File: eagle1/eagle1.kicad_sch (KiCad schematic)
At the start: 2 parts

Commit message: Select USB-C plug
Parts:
- J1, J2: Manufacturer (none) -> GlobTek, Inc.; Part Number (none) -> PLUG-USBC-121SMT-4BS2S
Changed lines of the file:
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@@
       (effects (font (size 1.27 1.27)) hide)
     )
-    (property "Datasheet" "" (at 104.775 94.615 0)
+    (property "Datasheet" "https://globtek.my.salesforce-sites.com/spec/pdf/2342616/d2760419" (at 104.775 94.615 0)
       (effects (font (size 1.27 1.27)) hide)
     )
-    (property "Manufacturer" "" (at 104.775 94.615 0)
-      (effects (font (size 1.27 1.27)))
+    (property "Manufacturer" "GlobTek, Inc." (at 104.775 94.615 0)
+      (effects (font (size 1.27 1.27)) hide)
     )
-    (property "Part Number" "" (at 104.775 94.615 0)
-      (effects (font (size 1.27 1.27)))
+    (property "Part Number" "PLUG-USBC-121SMT-4BS2S" (at 104.775 94.615 0)
+      (effects (font (size 1.27 1.27)) hide)
     )
-    (property "Description" "" (at 104.775 94.615 0)
-      (effects (font (size 1.27 1.27)))
+    (property "Description" "USB-C (USB TYPE-C) USB 2.0 Plug Connector 24 (12+12 Dummy) Position Surface Mount, Right Angle" (at 104.775 94.615 0)
+      (effects (font (size 1.27 1.27)) hide)
     )
     (pin "A1")
@@
       (effects (font (size 1.27 1.27)) hide)
     )
-    (property "Datasheet" "" (at 204.47 94.615 0)
+    (property "Datasheet" "https://globtek.my.salesforce-sites.com/spec/pdf/2342616/d2760419" (at 204.47 94.615 0)
       (effects (font (size 1.27 1.27)) hide)
     )
+    (property "Manufacturer" "GlobTek, Inc." (at 204.47 94.615 0)
+      (effects (font (size 1.27 1.27)) hide)
+    )
+    (property "Part Number" "PLUG-USBC-121SMT-4BS2S" (at 204.47 94.615 0)
+      (effects (font (size 1.27 1.27)) hide)
+    )
+    (property "Description" "USB-C (USB TYPE-C) USB 2.0 Plug Connector 24 (12+12 Dummy) Position Surface Mount, Right Angle" (at 204.47 94.615 0)
+      (effects (font (size 1.27 1.27)) hide)
+    )

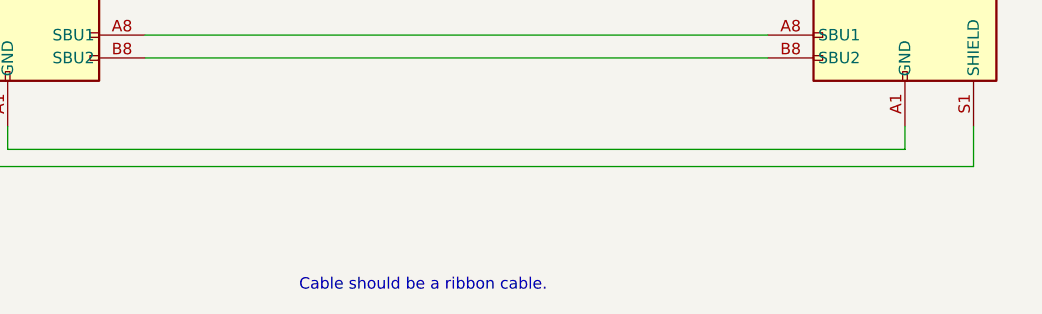
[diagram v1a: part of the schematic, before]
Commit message: Add footprint for Eagle1 USB-C plug
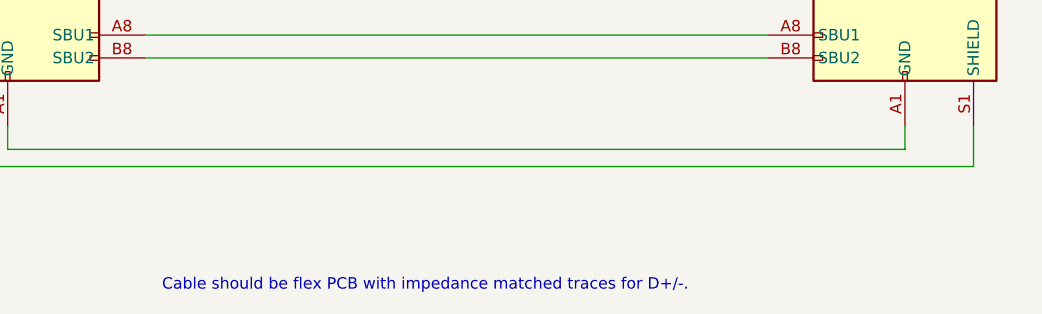
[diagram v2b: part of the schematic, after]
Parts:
- J1, J2: value ~ -> USB-C Plug; footprint (none) -> tycho:PLUG-USBC-121SMT
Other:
- note added: "Cable should be flex PCB with impedance matched traces for D+/-."
- note removed: "Cable should be a ribbon cable."
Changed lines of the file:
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@@
     (effects (font (size 1.27 1.27)) (justify left bottom))
   )
-  (text "Cable should be a ribbon cable." (at 137.16 146.05 0)
+  (text "Cable should be flex PCB with impedance matched traces for D+/-."
+    (at 121.92 146.05 0)
     (effects (font (size 1.27 1.27)) (justify left bottom))
   )
@@
       (effects (font (size 1.27 1.27)))
     )
-    (property "Value" "~" (at 104.775 94.615 0)
-      (effects (font (size 1.27 1.27)))
+    (property "Value" "USB-C Plug" (at 104.775 94.615 0)
+      (effects (font (size 1.27 1.27)) hide)
     )
-    (property "Footprint" "" (at 104.775 94.615 0)
+    (property "Footprint" "tycho:PLUG-USBC-121SMT" (at 104.775 94.615 0)
       (effects (font (size 1.27 1.27)) hide)
     )
@@
       (effects (font (size 1.27 1.27)) (justify right))
     )
-    (property "Value" "~" (at 204.47 94.615 0)
-      (effects (font (size 1.27 1.27)))
-    )
-    (property "Footprint" "" (at 204.47 94.615 0)
+    (property "Value" "USB-C Plug" (at 204.47 94.615 0)
       (effects (font (size 1.27 1.27)) hide)
     )
+    (property "Footprint" "tycho:PLUG-USBC-121SMT" (at 204.47 94.615 0)
+      (effects (font (size 1.27 1.27)) hide)
+    )

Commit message: Add footprint for U261-241N-4BC2LS USB-C plug
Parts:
- J1, J2: Manufacturer GlobTek, Inc. -> XKB Connectivity; Part Number PLUG-USBC-121SMT-4BS2S -> U261-241N-4BC2SS
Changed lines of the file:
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@@
       (effects (font (size 1.27 1.27)) hide)
     )
-    (property "Datasheet" "https://globtek.my.salesforce-sites.com/spec/pdf/2342616/d2760419" (at 104.775 94.615 0)
+    (property "Datasheet" "https://datasheet.lcsc.com/lcsc/2201121830_XKB-Connectivity-U261-241N-4BC2SS_C2938597.pdf" (at 104.775 94.615 0)
       (effects (font (size 1.27 1.27)) hide)
     )
-    (property "Manufacturer" "GlobTek, Inc." (at 104.775 94.615 0)
+    (property "Manufacturer" "XKB Connectivity" (at 104.775 94.615 0)
       (effects (font (size 1.27 1.27)) hide)
     )
-    (property "Part Number" "PLUG-USBC-121SMT-4BS2S" (at 104.775 94.615 0)
+    (property "Part Number" "U261-241N-4BC2SS" (at 104.775 94.615 0)
       (effects (font (size 1.27 1.27)) hide)
     )
-    (property "Description" "USB-C (USB TYPE-C) USB 2.0 Plug Connector 24 (12+12 Dummy) Position Surface Mount, Right Angle" (at 104.775 94.615 0)
+    (property "Description" "5A USB 3.1 1 260℃ Sink board 24P male -40℃~+85℃ Gold Copper Alloy Type-C SMD USB Connectors ROHS" (at 104.775 94.615 0)
       (effects (font (size 1.27 1.27)) hide)
     )
@@
       (effects (font (size 1.27 1.27)) hide)
     )
-    (property "Datasheet" "https://globtek.my.salesforce-sites.com/spec/pdf/2342616/d2760419" (at 204.47 94.615 0)
+    (property "Datasheet" "https://datasheet.lcsc.com/lcsc/2201121830_XKB-Connectivity-U261-241N-4BC2SS_C2938597.pdf" (at 204.47 94.615 0)
       (effects (font (size 1.27 1.27)) hide)
     )
-    (property "Manufacturer" "GlobTek, Inc." (at 204.47 94.615 0)
+    (property "Manufacturer" "XKB Connectivity" (at 204.47 94.615 0)
       (effects (font (size 1.27 1.27)) hide)
     )
-    (property "Part Number" "PLUG-USBC-121SMT-4BS2S" (at 204.47 94.615 0)
+    (property "Part Number" "U261-241N-4BC2SS" (at 204.47 94.615 0)
       (effects (font (size 1.27 1.27)) hide)
     )
-    (property "Description" "USB-C (USB TYPE-C) USB 2.0 Plug Connector 24 (12+12 Dummy) Position Surface Mount, Right Angle" (at 204.47 94.615 0)
+    (property "Description" "5A USB 3.1 1 260℃ Sink board 24P male -40℃~+85℃ Gold Copper Alloy Type-C SMD USB Connectors ROHS" (at 204.47 94.615 0)
       (effects (font (size 1.27 1.27)) hide)
     )

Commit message: Fix U261-241N-4BC2LS footprint; add U261-241N-4BC2LS to the schematic
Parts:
- J1, J2: footprint tycho:PLUG-USBC-121SMT -> tycho:U261-241N-4BC2LS; Part Number U261-241N-4BC2SS -> U261-241N-4BC2LS
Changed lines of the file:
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@@
       (effects (font (size 1.27 1.27)) hide)
     )
-    (property "Footprint" "tycho:PLUG-USBC-121SMT" (at 104.775 94.615 0)
+    (property "Footprint" "tycho:U261-241N-4BC2LS" (at 104.775 94.615 0)
       (effects (font (size 1.27 1.27)) hide)
     )
@@
       (effects (font (size 1.27 1.27)) hide)
     )
-    (property "Part Number" "U261-241N-4BC2SS" (at 104.775 94.615 0)
+    (property "Part Number" "U261-241N-4BC2LS" (at 104.775 94.615 0)
       (effects (font (size 1.27 1.27)) hide)
     )
@@
       (effects (font (size 1.27 1.27)) hide)
     )
-    (property "Footprint" "tycho:PLUG-USBC-121SMT" (at 204.47 94.615 0)
+    (property "Footprint" "tycho:U261-241N-4BC2LS" (at 204.47 94.615 0)
       (effects (font (size 1.27 1.27)) hide)
     )
@@
       (effects (font (size 1.27 1.27)) hide)
     )
-    (property "Part Number" "U261-241N-4BC2SS" (at 204.47 94.615 0)
+    (property "Part Number" "U261-241N-4BC2LS" (at 204.47 94.615 0)
       (effects (font (size 1.27 1.27)) hide)
     )

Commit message: Initial layout
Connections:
- net D+: now reaches J1.A6 (D+), J2.A6 (D+)
- net D+: now also J1.B6 (D+), J2.B6 (D+)
- net D-: now reaches J1.A7 (D-), J2.A7 (D-)
- net D-: now also J1.B7 (D-), J2.B7 (D-)
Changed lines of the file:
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@@
     (comment 1 "Licensed under the CERN-OHL-P v2")
+  )
+  (junction (at 123.19 79.375) (diameter 0) (color 0 0 0 0)
+  )
+  (junction (at 186.69 79.375) (diameter 0) (color 0 0 0 0)
+  )
+  (junction (at 186.69 74.295) (diameter 0) (color 0 0 0 0)
+  )
+  (junction (at 123.19 74.295) (diameter 0) (color 0 0 0 0)
   )
   (no_connect (at 120.015 89.535))
@@
   (no_connect (at 120.015 104.775))
   (no_connect (at 189.23 94.615))
+  (wire (pts (xy 120.015 76.835) (xy 123.19 76.835))
+    (stroke (width 0) (type default))
+  )
   (wire (pts (xy 120.015 120.015) (xy 189.23 120.015))
     (stroke (width 0) (type default))
   )
+  (wire (pts (xy 189.23 76.835) (xy 186.69 76.835))
+    (stroke (width 0) (type default))
+  )
+  (wire (pts (xy 120.015 81.915) (xy 123.19 81.915))
+    (stroke (width 0) (type default))
+  )
+  (wire (pts (xy 123.19 74.295) (xy 186.69 74.295))
+    (stroke (width 0) (type default))
+  )
   (wire (pts (xy 120.015 66.675) (xy 189.23 66.675))
     (stroke (width 0) (type default))
@@
     (stroke (width 0) (type default))
   )
+  (wire (pts (xy 123.19 79.375) (xy 186.69 79.375))
+    (stroke (width 0) (type default))
+  )
+  (wire (pts (xy 123.19 76.835) (xy 123.19 74.295))
+    (stroke (width 0) (type default))
+  )
   (wire (pts (xy 120.015 61.595) (xy 189.23 61.595))
     (stroke (width 0) (type default))
   )
+  (wire (pts (xy 120.015 74.295) (xy 123.19 74.295))
+    (stroke (width 0) (type default))
+  )
+  (wire (pts (xy 186.69 79.375) (xy 189.23 79.375))
+    (stroke (width 0) (type default))
+  )
+  (wire (pts (xy 186.69 81.915) (xy 186.69 79.375))
+    (stroke (width 0) (type default))
+  )
+  (wire (pts (xy 186.69 74.295) (xy 189.23 74.295))
+    (stroke (width 0) (type default))
+  )
   (wire (pts (xy 104.775 130.175) (xy 204.47 130.175))
     (stroke (width 0) (type default))
@@
     (stroke (width 0) (type default))
   )
+  (wire (pts (xy 186.69 76.835) (xy 186.69 74.295))
+    (stroke (width 0) (type default))
+  )
+  (wire (pts (xy 123.19 81.915) (xy 123.19 79.375))
+    (stroke (width 0) (type default))
+  )
+  (wire (pts (xy 189.23 81.915) (xy 186.69 81.915))
+    (stroke (width 0) (type default))
+  )
   (wire (pts (xy 120.015 69.215) (xy 189.23 69.215))
     (stroke (width 0) (type default))
@@
     (stroke (width 0) (type default))
   )
-  (wire (pts (xy 120.015 79.375) (xy 189.23 79.375))
-    (stroke (width 0) (type default))
-  )
-  (wire (pts (xy 120.015 74.295) (xy 189.23 74.295))
+  (wire (pts (xy 120.015 79.375) (xy 123.19 79.375))
     (stroke (width 0) (type default))
   )
@@
   (text "Cable should be flex PCB with impedance matched traces for D+/-."
     (at 121.92 146.05 0)
+    (effects (font (size 1.27 1.27)) (justify left bottom))
+  )
+  (label "D-" (at 123.19 74.295 0) (fields_autoplaced)
+    (effects (font (size 1.27 1.27)) (justify left bottom))
+  )
+  (label "D+" (at 123.19 79.375 0) (fields_autoplaced)
     (effects (font (size 1.27 1.27)) (justify left bottom))
   )
@@
     (pin "B9")
     (pin "S1")
+    (pin "B7")
+    (pin "B6")
     (instances
       (project "eagle1"
@@
     (pin "B9")
     (pin "S1")
+    (pin "B6")
+    (pin "B7")
     (instances
       (project "eagle1"

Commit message: layout wip
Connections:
- net D+: no longer J1.B6 (D+), J2.B6 (D+)
- net D-: no longer J1.B7 (D-), J2.B7 (D-)
- net GND: now reaches J1.A1 (GND), J1.A12 (GND), J1.B1 (GND), J1.B12 (GND), J2.A1 (GND), J2.A12 (GND), J2.B1 (GND), J2.B12 (GND)
- net GND: now also J1.S1 (SHIELD), J2.S1 (SHIELD)
- net CC2: now reaches J1.A11 (RX2+)
- net CC2: now also J1.B2 (TX2+), J1.B3 (TX2-), J1.B5 (CC2), J2.B2 (TX2+), J2.B3 (TX2-), J2.B5 (CC2)
- net SBU2: now reaches J1.A3 (TX1-)
- net SBU2: now also J1.B10 (RX1-), J1.B8 (SBU2), J2.B10 (RX1-), J2.B8 (SBU2)
- net VBUS: now reaches J1.A4 (VBUS), J1.A9 (VBUS), J1.B4 (VBUS), J1.B9 (VBUS), J2.A4 (VBUS), J2.A9 (VBUS), J2.B4 (VBUS), J2.B9 (VBUS)
- net VBUS: now also J1.B11 (RX1+), J2.B11 (RX1+)
- net CC1: now reaches J1.A5 (CC1), J2.A5 (CC1)
- net SBU1: now reaches J1.A8 (SBU1), J2.A8 (SBU1)
- no-connect marks 16 -> 10
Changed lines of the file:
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@@
     (comment 1 "Licensed under the CERN-OHL-P v2")
   )
-  (junction (at 123.19 79.375) (diameter 0) (color 0 0 0 0)
+  (junction (at 104.775 130.175) (diameter 0) (color 0 0 0 0)
   )
-  (junction (at 186.69 79.375) (diameter 0) (color 0 0 0 0)
+  (junction (at 187.325 109.855) (diameter 0) (color 0 0 0 0)
   )
-  (junction (at 186.69 74.295) (diameter 0) (color 0 0 0 0)
+  (junction (at 204.47 130.175) (diameter 0) (color 0 0 0 0)
   )
-  (junction (at 123.19 74.295) (diameter 0) (color 0 0 0 0)
+  (junction (at 187.325 69.215) (diameter 0) (color 0 0 0 0)
   )
-  (no_connect (at 120.015 89.535))
-  (no_connect (at 189.23 89.535))
-  (no_connect (at 120.015 94.615))
+  (junction (at 130.175 61.595) (diameter 0) (color 0 0 0 0)
+  )
+  (junction (at 182.88 61.595) (diameter 0) (color 0 0 0 0)
+  )
+  (junction (at 121.92 109.855) (diameter 0) (color 0 0 0 0)
+  )
+  (junction (at 123.19 120.015) (diameter 0) (color 0 0 0 0)
+  )
+  (junction (at 123.19 94.615) (diameter 0) (color 0 0 0 0)
+  )
+  (junction (at 179.705 120.015) (diameter 0) (color 0 0 0 0)
+  )
+  (junction (at 121.92 104.775) (diameter 0) (color 0 0 0 0)
+  )
+  (junction (at 121.92 69.215) (diameter 0) (color 0 0 0 0)
+  )
+  (no_connect (at 120.015 76.835))
   (no_connect (at 189.23 102.235))
-  (no_connect (at 120.015 109.855))
+  (no_connect (at 189.23 81.915))
   (no_connect (at 120.015 102.235))
-  (no_connect (at 120.015 86.995))
-  (no_connect (at 189.23 109.855))
-  (no_connect (at 120.015 112.395))
   (no_connect (at 120.015 97.155))
-  (no_connect (at 189.23 112.395))
-  (no_connect (at 189.23 86.995))
+  (no_connect (at 120.015 81.915))
   (no_connect (at 189.23 104.775))
   (no_connect (at 189.23 97.155))
-  (no_connect (at 120.015 104.775))
+  (no_connect (at 189.23 76.835))
   (no_connect (at 189.23 94.615))
-  (wire (pts (xy 120.015 76.835) (xy 123.19 76.835))
+  (wire (pts (xy 187.325 109.855) (xy 187.325 112.395))
     (stroke (width 0) (type default))
   )
-  (wire (pts (xy 120.015 120.015) (xy 189.23 120.015))
+  (wire (pts (xy 187.325 112.395) (xy 189.23 112.395))
     (stroke (width 0) (type default))
   )
-  (wire (pts (xy 189.23 76.835) (xy 186.69 76.835))
+  (wire (pts (xy 179.705 120.015) (xy 189.23 120.015))
     (stroke (width 0) (type default))
   )
-  (wire (pts (xy 120.015 81.915) (xy 123.19 81.915))
+  (wire (pts (xy 120.015 104.775) (xy 121.92 104.775))
     (stroke (width 0) (type default))
   )
-  (wire (pts (xy 123.19 74.295) (xy 186.69 74.295))
+  (wire (pts (xy 120.015 120.015) (xy 123.19 120.015))
+    (stroke (width 0) (type default))
+  )
+  (wire (pts (xy 120.015 94.615) (xy 123.19 94.615))
+    (stroke (width 0) (type default))
+  )
+  (wire (pts (xy 121.92 109.855) (xy 121.92 112.395))
+    (stroke (width 0) (type default))
+  )
+  (wire (pts (xy 120.015 109.855) (xy 121.92 109.855))
+    (stroke (width 0) (type default))
+  )
+  (wire (pts (xy 179.705 86.995) (xy 189.23 86.995))
+    (stroke (width 0) (type default))
+  )
+  (wire (pts (xy 120.015 89.535) (xy 130.175 89.535))
+    (stroke (width 0) (type default))
+  )
+  (wire (pts (xy 130.175 61.595) (xy 182.88 61.595))
     (stroke (width 0) (type default))
   )
@@
     (stroke (width 0) (type default))
   )
-  (wire (pts (xy 120.015 117.475) (xy 189.23 117.475))
+  (wire (pts (xy 121.92 104.775) (xy 121.92 109.855))
     (stroke (width 0) (type default))
   )
-  (wire (pts (xy 123.19 79.375) (xy 186.69 79.375))
+  (wire (pts (xy 120.015 79.375) (xy 189.23 79.375))
     (stroke (width 0) (type default))
   )
-  (wire (pts (xy 123.19 76.835) (xy 123.19 74.295))
+  (wire (pts (xy 121.92 69.215) (xy 121.92 104.775))
     (stroke (width 0) (type default))
   )
-  (wire (pts (xy 120.015 61.595) (xy 189.23 61.595))
+  (wire (pts (xy 120.015 61.595) (xy 130.175 61.595))
     (stroke (width 0) (type default))
   )
-  (wire (pts (xy 120.015 74.295) (xy 123.19 74.295))
+  (wire (pts (xy 187.325 69.215) (xy 187.325 109.855))
     (stroke (width 0) (type default))
   )
-  (wire (pts (xy 186.69 79.375) (xy 189.23 79.375))
+  (wire (pts (xy 120.015 74.295) (xy 189.23 74.295))
     (stroke (width 0) (type default))
   )
-  (wire (pts (xy 186.69 81.915) (xy 186.69 79.375))
+  (wire (pts (xy 204.47 130.175) (xy 212.09 130.175))
     (stroke (width 0) (type default))
   )
-  (wire (pts (xy 186.69 74.295) (xy 189.23 74.295))
+  (wire (pts (xy 121.92 69.215) (xy 187.325 69.215))
+    (stroke (width 0) (type default))
+  )
+  (wire (pts (xy 182.88 89.535) (xy 182.88 61.595))
     (stroke (width 0) (type default))
   )
@@
     (stroke (width 0) (type default))
   )
-  (wire (pts (xy 97.155 127.635) (xy 97.155 132.08))
+  (wire (pts (xy 97.155 127.635) (xy 97.155 130.175))
     (stroke (width 0) (type default))
   )
-  (wire (pts (xy 186.69 76.835) (xy 186.69 74.295))
+  (wire (pts (xy 187.325 109.855) (xy 189.23 109.855))
     (stroke (width 0) (type default))
   )
-  (wire (pts (xy 123.19 81.915) (xy 123.19 79.375))
+  (wire (pts (xy 123.19 86.995) (xy 123.19 94.615))
     (stroke (width 0) (type default))
   )
-  (wire (pts (xy 189.23 81.915) (xy 186.69 81.915))
+  (wire (pts (xy 189.23 89.535) (xy 182.88 89.535))
     (stroke (width 0) (type default))
   )
-  (wire (pts (xy 120.015 69.215) (xy 189.23 69.215))
+  (wire (pts (xy 187.325 69.215) (xy 189.23 69.215))
     (stroke (width 0) (type default))
   )
-  (wire (pts (xy 212.09 132.08) (xy 212.09 127.635))
+  (wire (pts (xy 179.705 86.995) (xy 179.705 120.015))
     (stroke (width 0) (type default))
   )
-  (wire (pts (xy 120.015 79.375) (xy 123.19 79.375))
+  (wire (pts (xy 121.92 112.395) (xy 120.015 112.395))
     (stroke (width 0) (type default))
   )
-  (wire (pts (xy 97.155 132.08) (xy 212.09 132.08))
+  (wire (pts (xy 123.19 94.615) (xy 123.19 120.015))
+    (stroke (width 0) (type default))
+  )
+  (wire (pts (xy 130.175 61.595) (xy 130.175 89.535))
+    (stroke (width 0) (type default))
+  )
+  (wire (pts (xy 120.015 117.475) (xy 189.23 117.475))
+    (stroke (width 0) (type default))
+  )
+  (wire (pts (xy 120.015 69.215) (xy 121.92 69.215))
+    (stroke (width 0) (type default))
+  )
+  (wire (pts (xy 120.015 86.995) (xy 123.19 86.995))
+    (stroke (width 0) (type default))
+  )
+  (wire (pts (xy 212.09 130.175) (xy 212.09 127.635))
+    (stroke (width 0) (type default))
+  )
+  (wire (pts (xy 123.19 120.015) (xy 179.705 120.015))
+    (stroke (width 0) (type default))
+  )
+  (wire (pts (xy 182.88 61.595) (xy 189.23 61.595))
+    (stroke (width 0) (type default))
+  )
+  (wire (pts (xy 97.155 130.175) (xy 104.775 130.175))
     (stroke (width 0) (type default))
   )
@@
     (effects (font (size 1.27 1.27)) (justify left bottom))
   )
+  (label "CC2" (at 121.92 69.215 0) (fields_autoplaced)
+    (effects (font (size 1.27 1.27)) (justify left bottom))
+  )
+  (label "VBUS" (at 130.175 61.595 0) (fields_autoplaced)
+    (effects (font (size 1.27 1.27)) (justify left bottom))
+  )
+  (label "SBU1" (at 125.095 117.475 0) (fields_autoplaced)
+    (effects (font (size 1.27 1.27)) (justify left bottom))
+  )
+  (label "GND" (at 109.855 130.175 0) (fields_autoplaced)
+    (effects (font (size 1.27 1.27)) (justify left bottom))
+  )
+  (label "SBU2" (at 125.095 120.015 0) (fields_autoplaced)
+    (effects (font (size 1.27 1.27)) (justify left bottom))
+  )
   (label "D-" (at 123.19 74.295 0) (fields_autoplaced)
     (effects (font (size 1.27 1.27)) (justify left bottom))
@@
     (effects (font (size 1.27 1.27)) (justify left bottom))
   )
+  (label "CC1" (at 121.92 66.675 0) (fields_autoplaced)
+    (effects (font (size 1.27 1.27)) (justify left bottom))
+  )
